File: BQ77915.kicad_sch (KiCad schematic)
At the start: 18 parts, among them U1 BQ7791500PWR

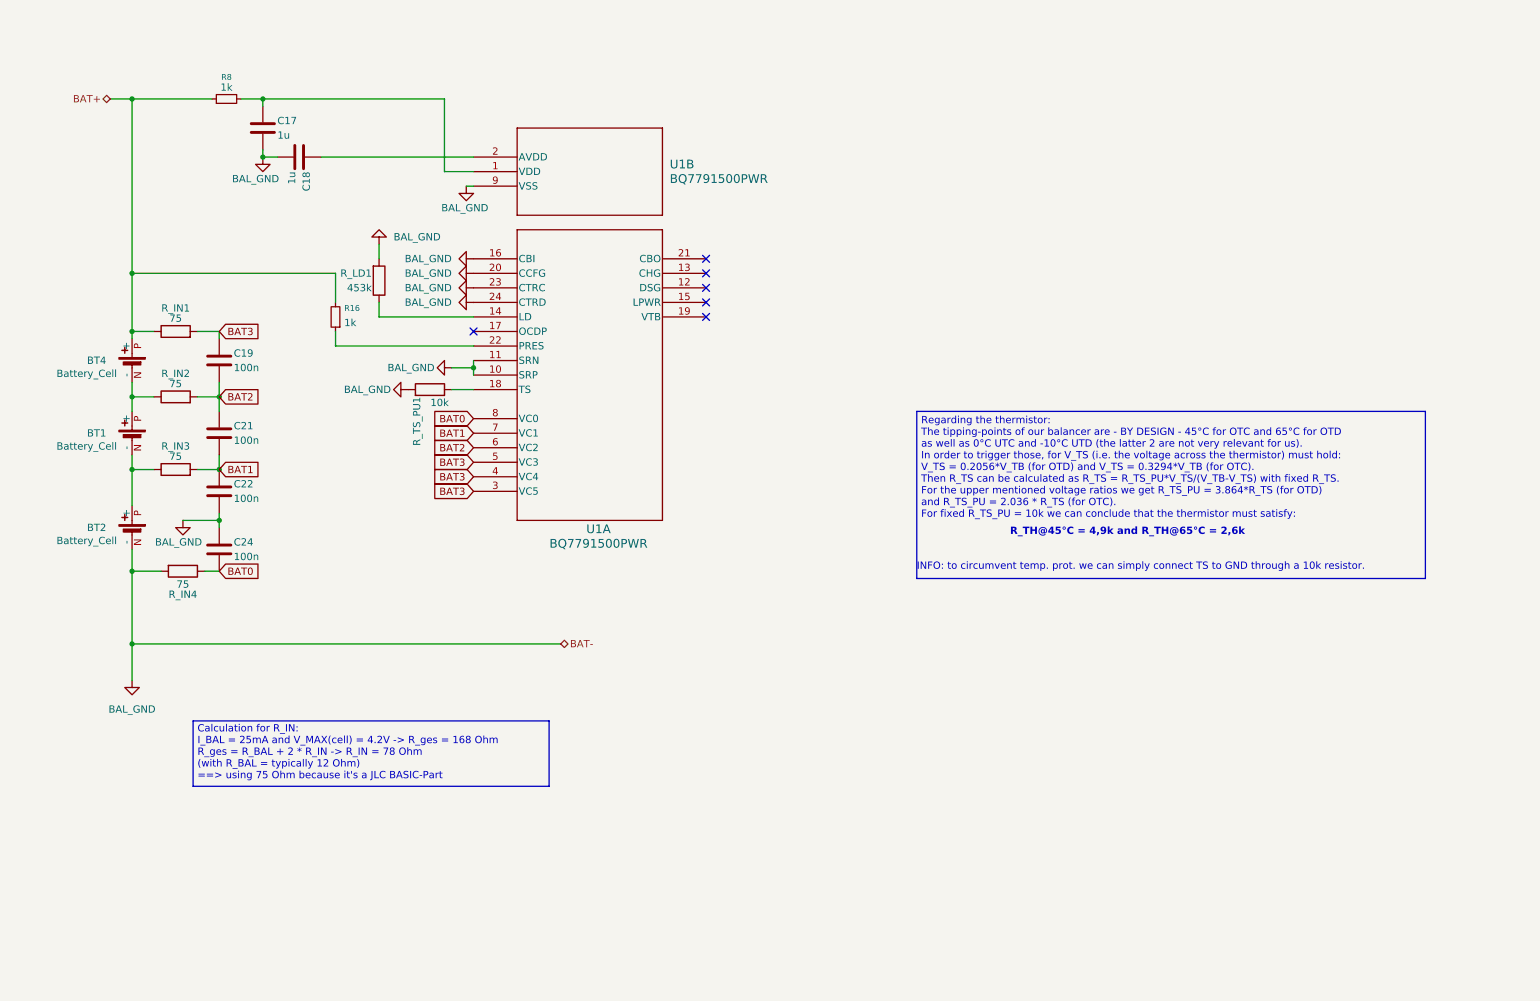
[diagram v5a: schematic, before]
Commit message: added current sensing circuit
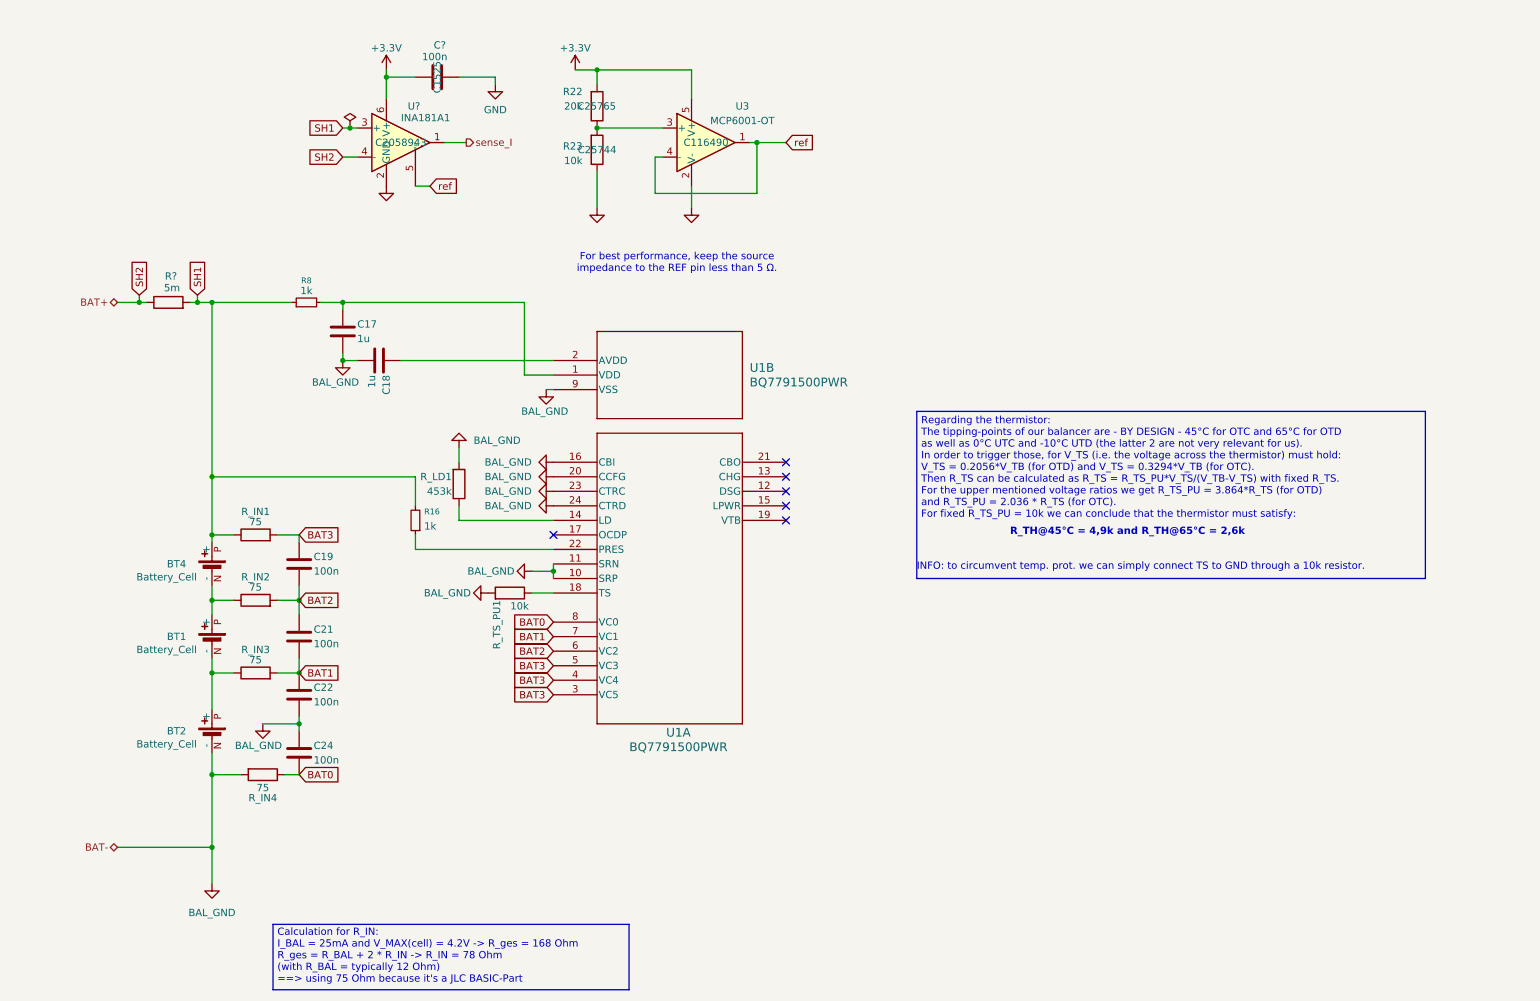
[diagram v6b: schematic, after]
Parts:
- added C?: 100n, Capacitor_SMD:C_0402_1005Metric, symbol Device:C
- added R22: 20k, Resistor_SMD:R_0402_1005Metric_Pad0.72x0.64mm_HandSolder, symbol Device:R
- added R23: 10k, Resistor_SMD:R_0402_1005Metric_Pad0.72x0.64mm_HandSolder, symbol Device:R
- added R?: 5m, Resistor_SMD:R_2512_6332Metric_Pad1.40x3.35mm_HandSolder, symbol Device:R
- added U3: MCP6001-OT, Package_TO_SOT_SMD:SOT-23-5, symbol Amplifier_Operational:MCP6001-OT
- added U?: INA181A1, Package_TO_SOT_SMD:SOT-23-6, symbol Amplifier_Current:INA181
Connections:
- net BAT+ renamed SH1
- net SH1: now also R?.2, U?.3 (+)
- new net: R22.1, R23.2, U3.3 (+)
- new net +3.3V: C?.1, R22.2, U3.5 (V+), U?.6 (V+)
- new net GND: C?.2, R23.1, U3.2 (V-), U?.2 (GND)
- new net SH2: R?.1, U?.4 (-)
- new net ref: U3.1, U3.4 (-), U?.5 (REF)
- new net sense_I: U?.1
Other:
- note added: "For best performance, keep the source impedance to the REF pin less than 5 Ω."
- moved on the sheet: BT1, BT2, BT4, C17, C18, C19, C21, C22, C24, R16, R8, R_IN1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

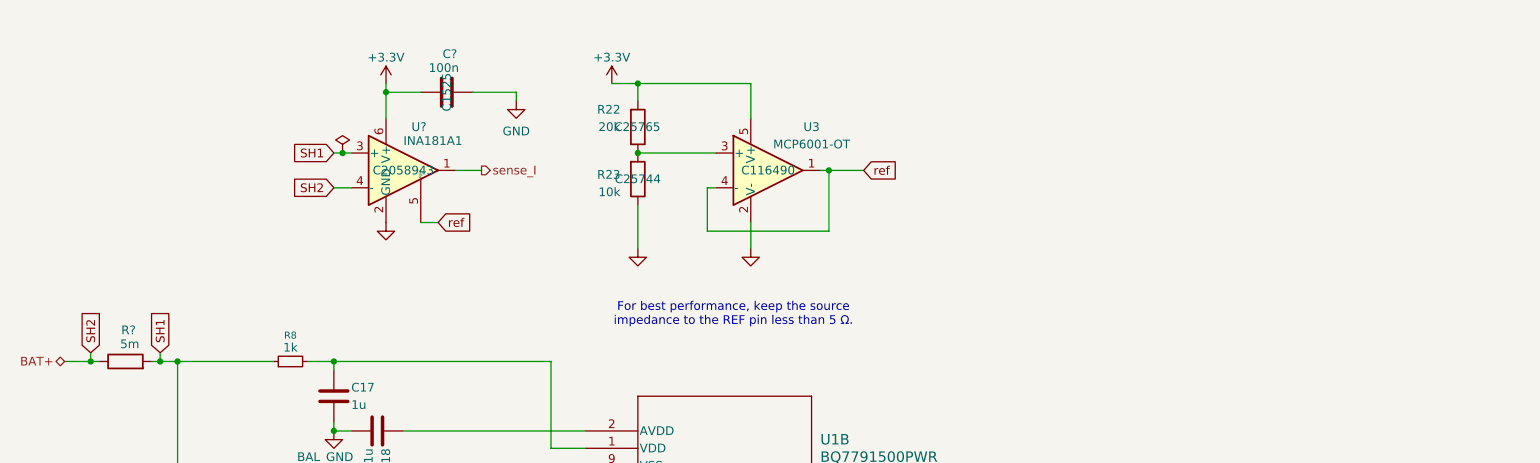
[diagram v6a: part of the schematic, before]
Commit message: finished adding sensing-capabilities (incl. routing)
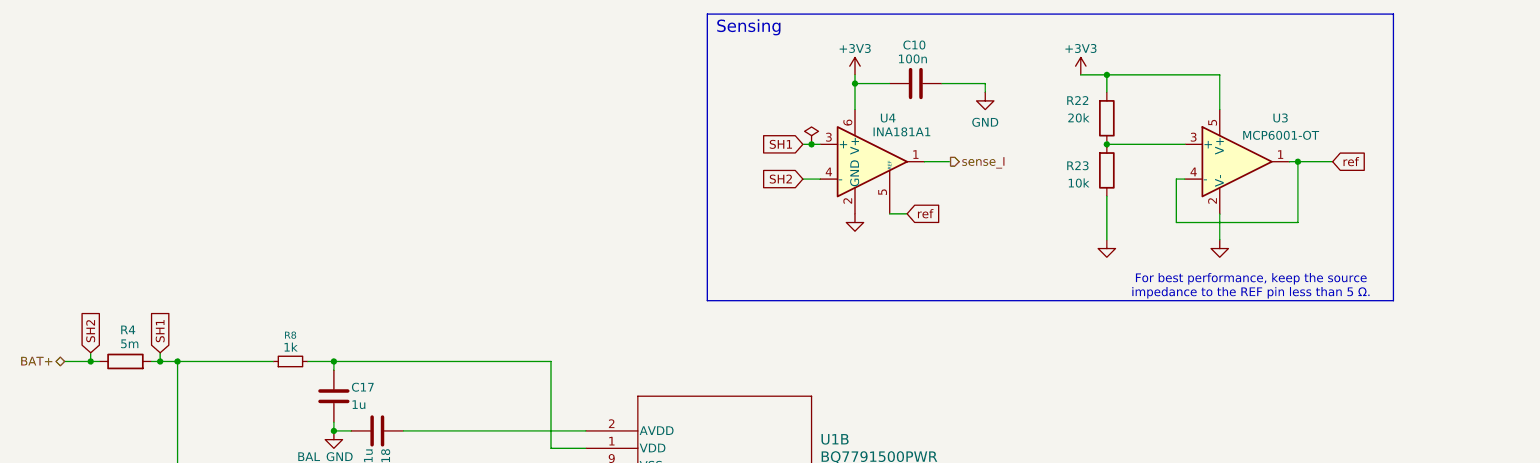
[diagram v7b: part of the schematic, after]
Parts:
- gave numbers to parts that had none: 3
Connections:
- net +3.3V renamed +3V3
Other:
- note added: "Sensing"
- moved on the sheet: C10, R22, R23, U3, U4

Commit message: preparing for order
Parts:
- BT1, BT2: now not fitted
- BT3: renamed from BT4; now not fitted
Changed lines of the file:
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@@
 		(in_bom yes)
 		(on_board yes)
-		(dnp no)
+		(dnp yes)
 		(property "Reference" "BT2"
 			(at 54.356 142.24 0)
@@
 		(in_bom yes)
 		(on_board yes)
-		(dnp no)
-		(property "Reference" "BT4"
+		(dnp yes)
+		(property "Reference" "BT3"
 			(at 54.356 113.03 0)
 			(effects
@@
 			(project "rapid_power_module"
 				(path "/afc8cbd3-9ea8-40a2-afae-ed6bd0fe7e6e/f9ba2c7f-e63c-4860-86c8-ae922535c6b3"
-					(reference "BT4")
+					(reference "BT3")
 					(unit 1)
 				)
@@
 		(in_bom yes)
 		(on_board yes)
-		(dnp no)
+		(dnp yes)
 		(property "Reference" "BT1"
 			(at 54.356 125.73 0)
